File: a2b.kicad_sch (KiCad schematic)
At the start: 15 parts, among them SW1 SW_DIP_x03, SW2 SW_DIP_x03, SW3 SW_DIP_x02

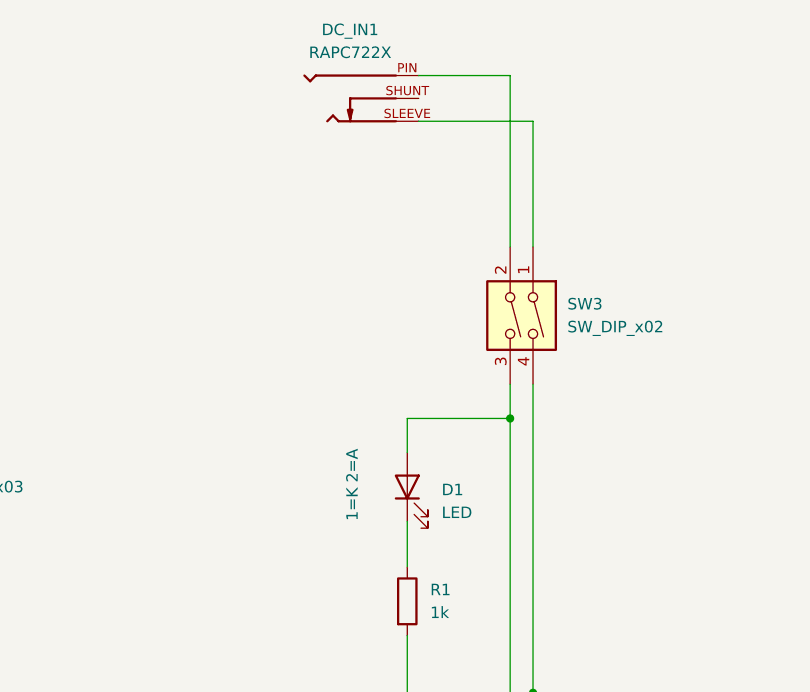
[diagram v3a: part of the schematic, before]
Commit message: added silkscreen
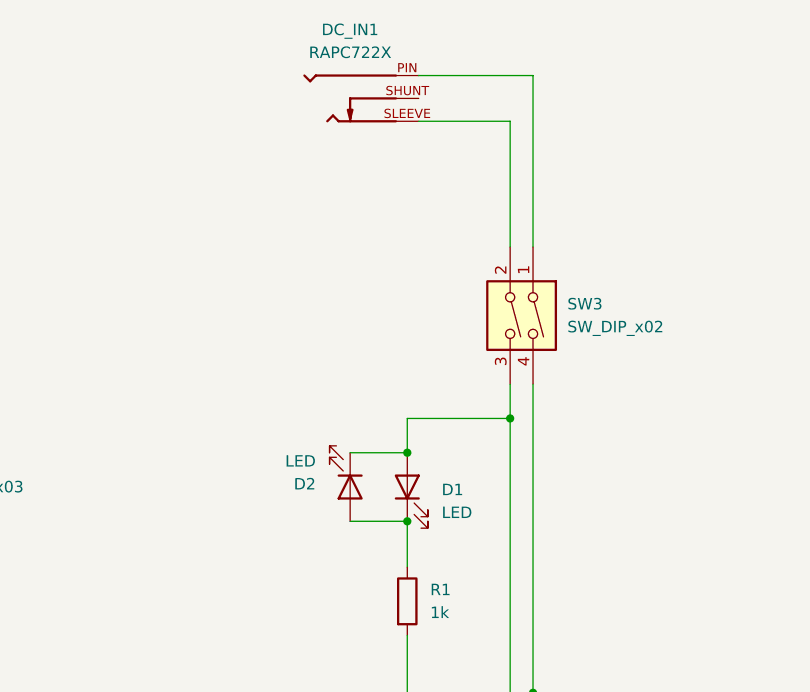
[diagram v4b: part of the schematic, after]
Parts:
- added D2: LED, LED_THT:LED_D5.0mm, symbol Device:LED
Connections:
- net at SW3.1: now also DC_IN1.PIN; no longer DC_IN1.SLEEVE
- net at SW3.2: now also DC_IN1.SLEEVE; no longer DC_IN1.PIN
- net at D1.2 (A), SW3.3, V1.2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: now also D2.1 (K)
- net at D1.1 (K), R1.1: now also D2.2 (A)
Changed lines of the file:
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@@
+	)
+	(junction
+		(at 133.35 83.82)
+		(diameter 0)
+		(color 0 0 0 0)
+	)
+	(junction
+		(at 133.35 91.44)
+		(diameter 0)
+		(color 0 0 0 0)
 	)
 	(junction
@@
 	(wire
 		(pts
+			(xy 127 91.44) (xy 133.35 91.44)
+		)
+		(stroke
+			(width 0)
+			(type default)
+		)
+	)
+	(wire
+		(pts
 			(xy 144.78 119.38) (xy 172.72 119.38)
 		)
@@
 	(wire
 		(pts
+			(xy 144.78 46.99) (xy 144.78 60.96)
+		)
+		(stroke
+			(width 0)
+			(type default)
+		)
+	)
+	(wire
+		(pts
 			(xy 71.12 116.84) (xy 71.12 127)
 		)
@@
 	(wire
 		(pts
-			(xy 134.62 41.91) (xy 144.78 41.91)
+			(xy 134.62 41.91) (xy 147.32 41.91)
 		)
 		(stroke
@@
 	(wire
 		(pts
-			(xy 144.78 41.91) (xy 144.78 60.96)
+			(xy 127 83.82) (xy 133.35 83.82)
 		)
 		(stroke
@@
 	(wire
 		(pts
-			(xy 147.32 46.99) (xy 147.32 60.96)
-		)
-		(stroke
-			(width 0)
-			(type default)
-		)
-	)
-	(wire
-		(pts
 			(xy 66.04 63.5) (xy 71.12 63.5)
 		)
@@
 	(wire
 		(pts
+			(xy 134.62 46.99) (xy 144.78 46.99)
+		)
+		(stroke
+			(width 0)
+			(type default)
+		)
+	)
+	(wire
+		(pts
 			(xy 219.71 119.38) (xy 223.52 119.38)
 		)
@@
 	(wire
 		(pts
-			(xy 134.62 46.99) (xy 147.32 46.99)
-		)
-		(stroke
-			(width 0)
-			(type default)
-		)
-	)
-	(wire
-		(pts
 			(xy 233.68 127) (xy 233.68 121.92)
 		)
@@
 		(pts
 			(xy 124.46 127) (xy 124.46 119.38)
+		)
+		(stroke
+			(width 0)
+			(type default)
+		)
+	)
+	(wire
+		(pts
+			(xy 147.32 41.91) (xy 147.32 60.96)
 		)
 		(stroke
@@
 				(path "/2fb67ef4-3b78-48fd-981f-3213cdbc031d"
 					(reference "SW3")
+					(unit 1)
+				)
+			)
+		)
+	)
+	(symbol
+		(lib_id "Device:LED")
+		(at 127 87.63 270)
+		(unit 1)
+		(body_style 1)
+		(exclude_from_sim no)
+		(in_bom yes)
+		(on_board yes)
+		(in_pos_files yes)
+		(dnp no)
+		(property "Reference" "D2"
+			(at 123.19 87.3126 90)
+			(show_name no)
+			(do_not_autoplace no)
+			(effects
+				(font
+					(size 1.27 1.27)
+				)
+				(justify right)
+			)
+		)
+		(property "Value" "LED"
+			(at 123.19 84.7726 90)
+			(show_name no)
+			(do_not_autoplace no)
+			(effects
+				(font
+					(size 1.27 1.27)
+				)
+				(justify right)
+			)
+		)
+		(property "Footprint" "LED_THT:LED_D5.0mm"
+			(at 127 87.63 0)
+			(hide yes)
+			(show_name no)
+			(do_not_autoplace no)
+			(effects
+				(font
+					(size 1.27 1.27)
+				)
+			)
+		)
+		(property "Datasheet" ""
+			(at 127 87.63 0)
+			(hide yes)
+			(show_name no)
+			(do_not_autoplace no)
+			(effects
+				(font
+					(size 1.27 1.27)
+				)
+			)
+		)
+		(property "Description" "Light emitting diode"
+			(at 127 87.63 0)
+			(hide yes)
+			(show_name no)
+			(do_not_autoplace no)
+			(effects
+				(font
+					(size 1.27 1.27)
+				)
+			)
+		)
+		(property "Sim.Pins" "1=K 2=A"
+			(at 149.352 87.122 0)
+			(hide yes)
+			(show_name no)
+			(do_not_autoplace no)
+			(effects
+				(font
+					(size 1.27 1.27)
+				)
+			)
+		)
+		(pin "2"
+		)
+		(pin "1"
+		)
+		(instances
+			(project "a2b"
+				(path "/2fb67ef4-3b78-48fd-981f-3213cdbc031d"
+					(reference "D2")
 					(unit 1)
 				)
@@
 		)
 		(property "Sim.Pins" "1=K 2=A"
-			(at 127.254 87.376 0)
-			(show_name no)
-			(do_not_autoplace no)
+			(at 110.998 88.138 0)
+			(hide yes)
+			(show_name no)
+			(do_not_autoplace no)

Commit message: sync board
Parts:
- renumbered AUDIO_IN1 to AUDIO_1, AUDIO_OUT1 to AUDIO_2
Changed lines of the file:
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@@
 		(dnp no)
 		(fields_autoplaced yes)
-		(property "Reference" "AUDIO_OUT1"
+		(property "Reference" "AUDIO_2"
 			(at 241.3 55.8799 0)
 			(show_name no)
@@
 			(project "a2b"
 				(path "/2fb67ef4-3b78-48fd-981f-3213cdbc031d"
-					(reference "AUDIO_OUT1")
+					(reference "AUDIO_2")
 					(unit 1)
 				)
@@
 		(dnp no)
 		(fields_autoplaced yes)
-		(property "Reference" "AUDIO_IN1"
+		(property "Reference" "AUDIO_1"
 			(at 59.055 46.99 0)
 			(show_name no)
@@
 			(project "a2b"
 				(path "/2fb67ef4-3b78-48fd-981f-3213cdbc031d"
-					(reference "AUDIO_IN1")
+					(reference "AUDIO_1")
 					(unit 1)
 				)
